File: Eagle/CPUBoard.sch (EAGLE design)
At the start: 33 parts, among them IC2 MAX232, IC3 MAX485CPA, J1 DISPLAY, J2 BUTTON_BOARD, J3 RELAY_BOARD, Q1 12.000MHz, X6 MKDSN1,5/3-5,08, X7 MKDSN1,5/3-5,08

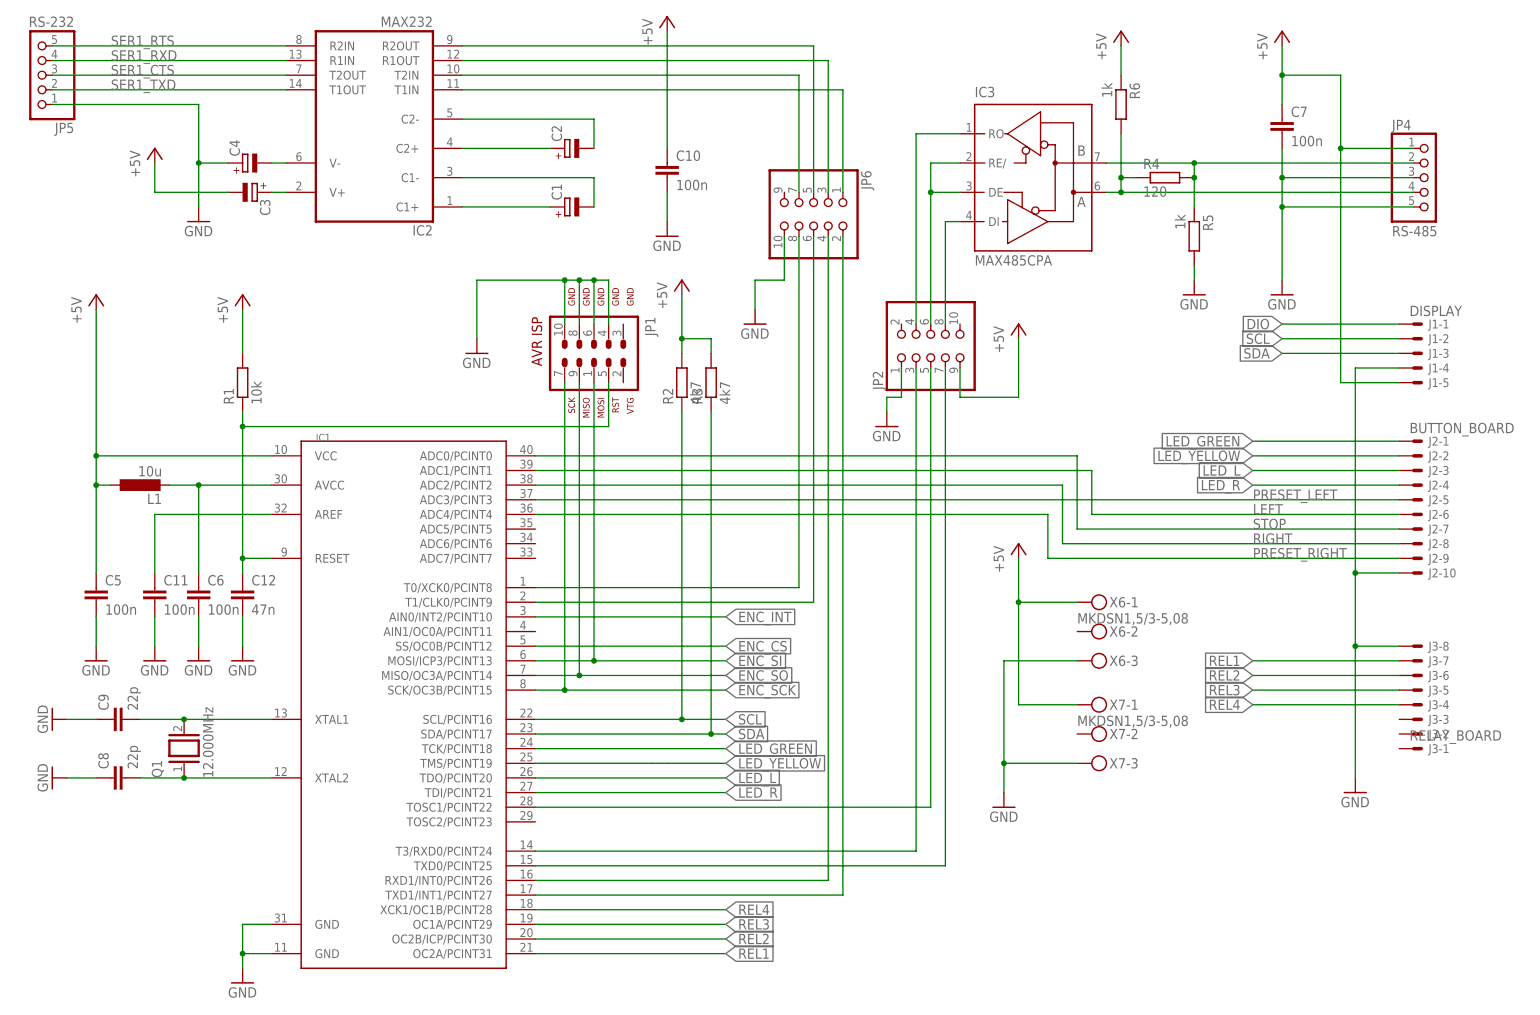
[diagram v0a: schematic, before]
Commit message: - wiring from/to MAX232 changed slightly
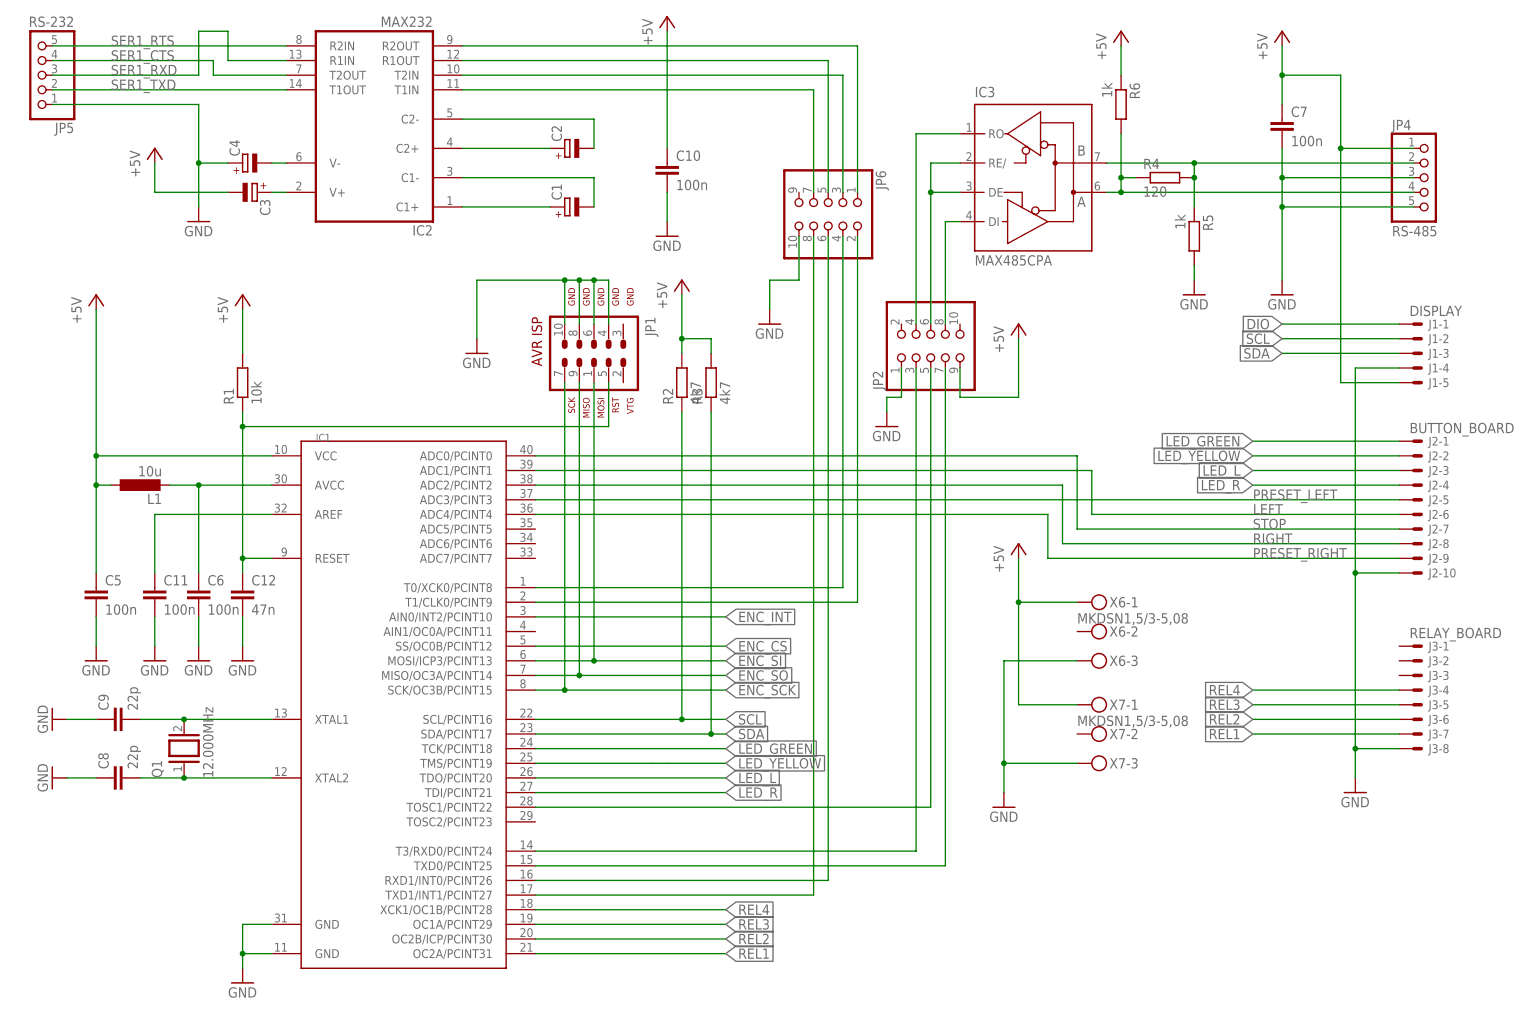
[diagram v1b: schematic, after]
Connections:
- removed net N$30: IC1.T1/CLK0/PCINT9, JP6.6
- removed net N$31: IC1.T0/XCK0/PCINT8, JP6.8
- new net N$22: IC1.RXD1/INT0/PCINT26, JP6.6
- new net N$25: IC1.T1/CLK0/PCINT9, JP6.2
- net N$11: now also JP6.5; no longer JP6.3
- net N$16: now also IC1.T0/XCK0/PCINT8; no longer IC1.RXD1/INT0/PCINT26
- net N$24: now also JP6.8; no longer JP6.2
- net N$28: now also JP6.1; no longer JP6.5
- net N$29: now also JP6.3; no longer JP6.7
- net N$4: now also JP6.7; no longer JP6.1
- net SER1_CTS: now also IC2G$1.R1IN; no longer IC2G$1.T2OUT
- net SER1_RXD: now also IC2G$1.T2OUT; no longer IC2G$1.R1IN
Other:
- moved on the sheet: J3-1, J3-2, J3-3, J3-4, J3-5, J3-6, J3-7, J3-8, JP6

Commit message: - another fix for the TWI pins, hopefully the last one!
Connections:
- net SCL: now also J1-3.S; no longer J1-2.S
- net SDA: now also J1-2.S; no longer J1-3.S
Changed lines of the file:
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@@
 </segment>
 <segment>
-<label x="220.98" y="121.92" size="1.778" layer="95" rot="MR0" xref="yes"/>
-<wire x1="241.3" y1="121.92" x2="220.98" y2="121.92" width="0.1524" layer="91"/>
-<pinref part="J1" gate="-2" pin="S"/>
+<label x="220.98" y="119.38" size="1.778" layer="95" rot="MR0" xref="yes"/>
+<wire x1="241.3" y1="119.38" x2="220.98" y2="119.38" width="0.1524" layer="91"/>
+<pinref part="J1" gate="-3" pin="S"/>
 </segment>
 </net>
@@
 </segment>
 <segment>
-<label x="220.98" y="119.38" size="1.778" layer="95" rot="MR0" xref="yes"/>
-<wire x1="241.3" y1="119.38" x2="220.98" y2="119.38" width="0.1524" layer="91"/>
-<pinref part="J1" gate="-3" pin="S"/>
+<label x="220.98" y="121.92" size="1.778" layer="95" rot="MR0" xref="yes"/>
+<pinref part="J1" gate="-2" pin="S"/>
+<wire x1="220.98" y1="121.92" x2="241.3" y2="121.92" width="0.1524" layer="91"/>
 </segment>
 </net>

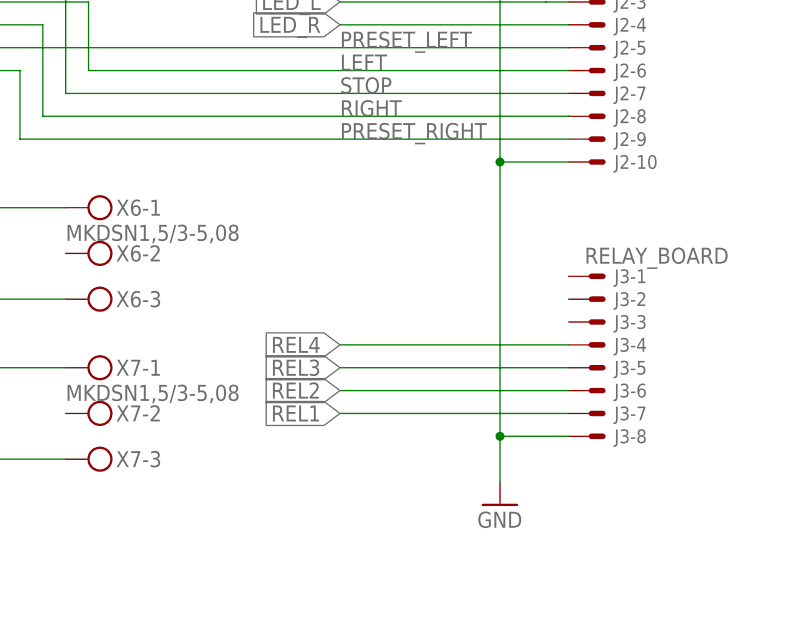
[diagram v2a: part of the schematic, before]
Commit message: - swapped connections to relay board1
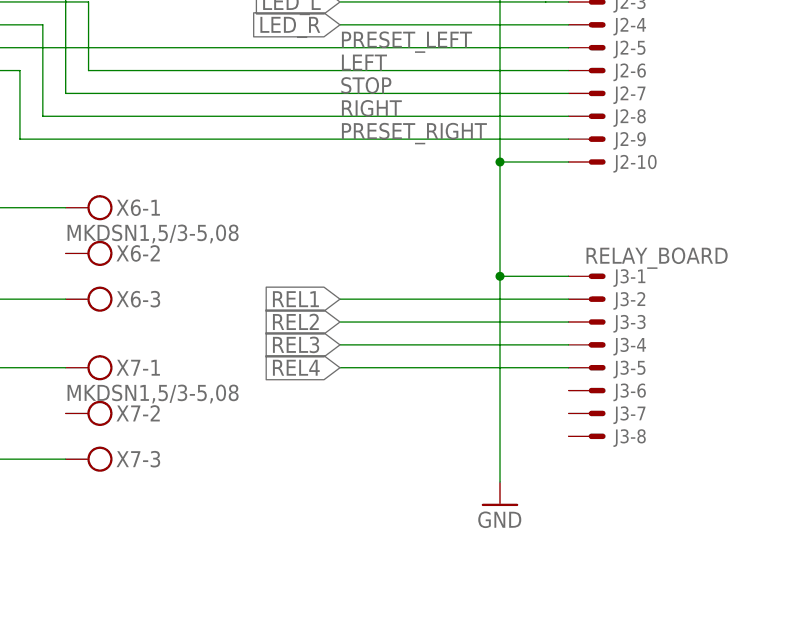
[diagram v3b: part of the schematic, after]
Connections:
- net GND: now also J3-1.S; no longer J3-8.S
- net REL1: now also J3-2.S; no longer J3-7.S
- net REL2: now also J3-3.S; no longer J3-6.S
- net REL3: now also J3-4.S; no longer J3-5.S
- net REL4: now also J3-5.S; no longer J3-4.S
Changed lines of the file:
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@@
 <segment>
 <pinref part="GND11" gate="1" pin="GND"/>
-<wire x1="233.68" y1="45.72" x2="233.68" y2="50.8" width="0.1524" layer="91"/>
-<wire x1="233.68" y1="50.8" x2="233.68" y2="81.28" width="0.1524" layer="91"/>
+<wire x1="233.68" y1="45.72" x2="233.68" y2="68.58" width="0.1524" layer="91"/>
+<wire x1="233.68" y1="68.58" x2="233.68" y2="81.28" width="0.1524" layer="91"/>
 <wire x1="241.3" y1="81.28" x2="233.68" y2="81.28" width="0.1524" layer="91"/>
 <wire x1="233.68" y1="116.84" x2="233.68" y2="81.28" width="0.1524" layer="91"/>
@@
 <pinref part="J1" gate="-4" pin="S"/>
 <pinref part="J2" gate="-10" pin="S"/>
-<pinref part="J3" gate="-8" pin="S"/>
-<wire x1="241.3" y1="50.8" x2="233.68" y2="50.8" width="0.1524" layer="91"/>
-<junction x="233.68" y="50.8"/>
+<pinref part="J3" gate="-1" pin="S"/>
+<wire x1="241.3" y1="68.58" x2="233.68" y2="68.58" width="0.1524" layer="91"/>
+<junction x="233.68" y="68.58"/>
 </segment>
 <segment>
@@
 <net name="REL1" class="0">
 <segment>
-<label x="215.9" y="53.34" size="1.778" layer="95" rot="MR0" xref="yes"/>
-<pinref part="J3" gate="-7" pin="S"/>
-<wire x1="215.9" y1="53.34" x2="241.3" y2="53.34" width="0.1524" layer="91"/>
+<label x="215.9" y="66.04" size="1.778" layer="95" rot="MR0" xref="yes"/>
+<pinref part="J3" gate="-2" pin="S"/>
+<wire x1="215.9" y1="66.04" x2="241.3" y2="66.04" width="0.1524" layer="91"/>
 </segment>
 <segment>
@@
 <net name="REL2" class="0">
 <segment>
-<label x="215.9" y="55.88" size="1.778" layer="95" rot="MR0" xref="yes"/>
-<pinref part="J3" gate="-6" pin="S"/>
-<wire x1="241.3" y1="55.88" x2="215.9" y2="55.88" width="0.1524" layer="91"/>
+<label x="215.9" y="63.5" size="1.778" layer="95" rot="MR0" xref="yes"/>
+<wire x1="241.3" y1="63.5" x2="215.9" y2="63.5" width="0.1524" layer="91"/>
+<pinref part="J3" gate="-3" pin="S"/>
 </segment>
 <segment>
@@
 <net name="REL3" class="0">
 <segment>
-<label x="215.9" y="58.42" size="1.778" layer="95" rot="MR0" xref="yes"/>
-<pinref part="J3" gate="-5" pin="S"/>
-<wire x1="215.9" y1="58.42" x2="241.3" y2="58.42" width="0.1524" layer="91"/>
+<label x="215.9" y="60.96" size="1.778" layer="95" rot="MR0" xref="yes"/>
+<pinref part="J3" gate="-4" pin="S"/>
+<wire x1="215.9" y1="60.96" x2="241.3" y2="60.96" width="0.1524" layer="91"/>
 </segment>
 <segment>
@@
 <net name="REL4" class="0">
 <segment>
-<label x="215.9" y="60.96" size="1.778" layer="95" rot="MR0" xref="yes"/>
-<pinref part="J3" gate="-4" pin="S"/>
-<wire x1="215.9" y1="60.96" x2="241.3" y2="60.96" width="0.1524" layer="91"/>
-</segment>
-<segment>
+<label x="215.9" y="58.42" size="1.778" layer="95" rot="MR0" xref="yes"/>
+<wire x1="215.9" y1="58.42" x2="241.3" y2="58.42" width="0.1524" layer="91"/>
+<pinref part="J3" gate="-5" pin="S"/>
+</segment>
+<segment>

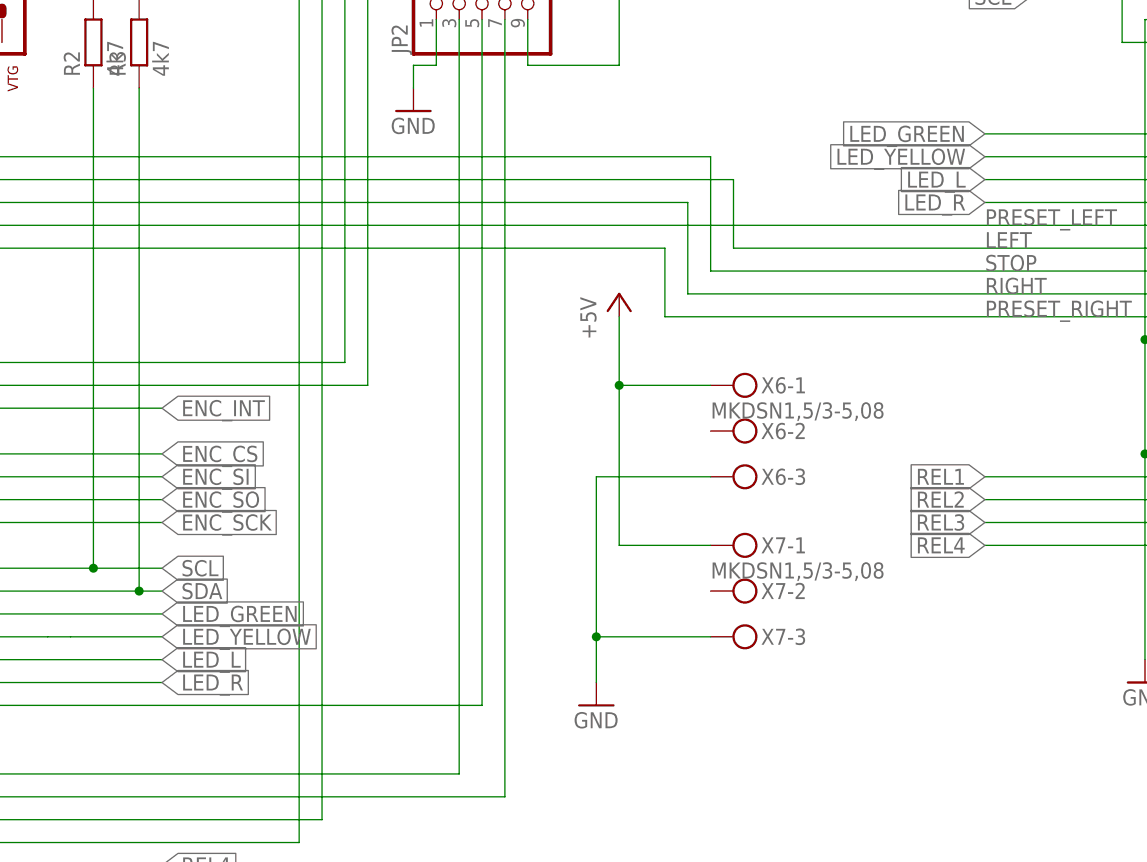
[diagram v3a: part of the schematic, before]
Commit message: - swapped LED_L and LED_R in schematic - solder bridge between two buttons found and fixed
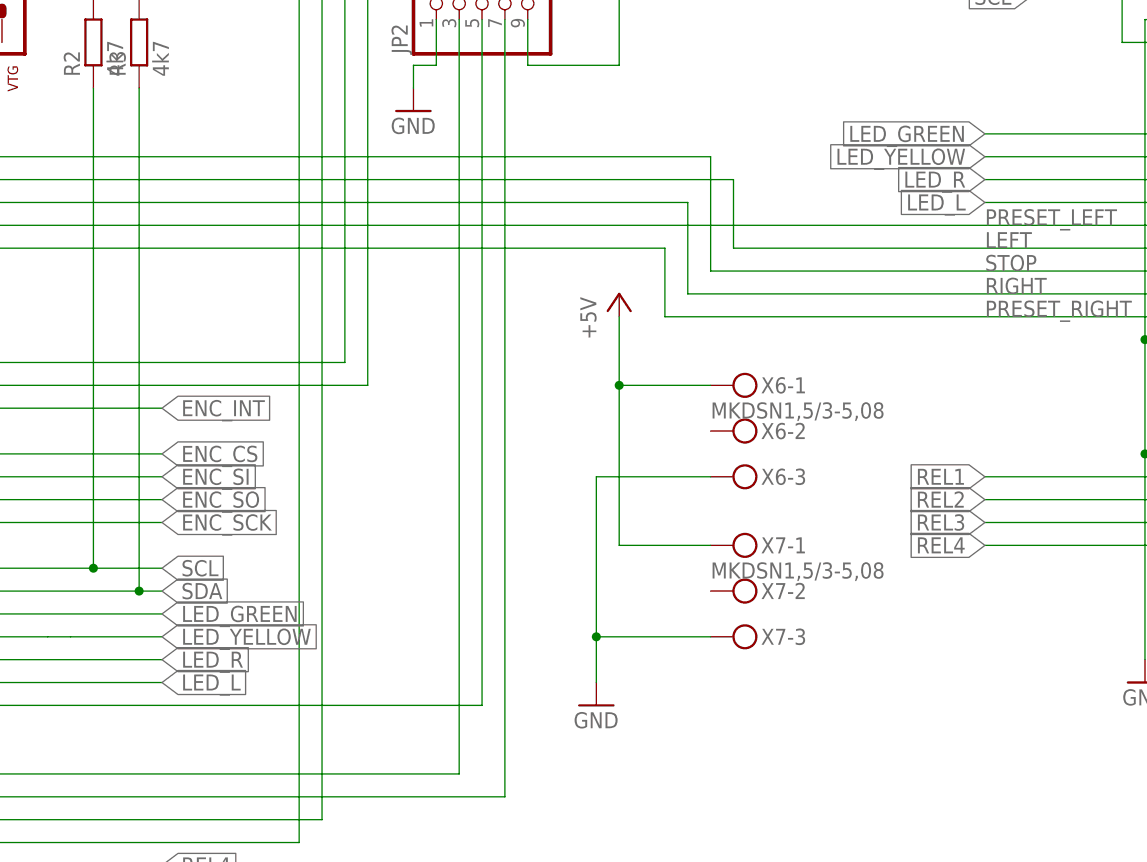
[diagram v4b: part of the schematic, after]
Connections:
- net LED_L: now also IC1.TDI/PCINT21, J2-4.S; no longer IC1.TDO/PCINT20, J2-3.S
- net LED_R: now also IC1.TDO/PCINT20, J2-3.S; no longer IC1.TDI/PCINT21, J2-4.S
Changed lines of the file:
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@@
 <net name="LED_L" class="0">
+<segment>
+<label x="124.46" y="43.18" size="1.778" layer="95" xref="yes"/>
+<pinref part="IC1" gate="G$1" pin="TDI/PCINT21"/>
+<wire x1="91.44" y1="43.18" x2="124.46" y2="43.18" width="0.1524" layer="91"/>
+</segment>
+<segment>
+<wire x1="241.3" y1="96.52" x2="215.9" y2="96.52" width="0.1524" layer="91"/>
+<label x="215.9" y="96.52" size="1.778" layer="95" rot="MR0" xref="yes"/>
+<pinref part="J2" gate="-4" pin="S"/>
+</segment>
+</net>
+<net name="LED_R" class="0">
+<segment>
+<wire x1="91.44" y1="45.72" x2="124.46" y2="45.72" width="0.1524" layer="91"/>
+<label x="124.46" y="45.72" size="1.778" layer="95" xref="yes"/>
+<pinref part="IC1" gate="G$1" pin="TDO/PCINT20"/>
+</segment>
 <segment>
 <wire x1="241.3" y1="99.06" x2="238.76" y2="99.06" width="0.1524" layer="91"/>
@@
 <wire x1="238.76" y1="99.06" x2="215.9" y2="99.06" width="0.1524" layer="91"/>
 </segment>
-<segment>
-<wire x1="91.44" y1="45.72" x2="124.46" y2="45.72" width="0.1524" layer="91"/>
-<label x="124.46" y="45.72" size="1.778" layer="95" xref="yes"/>
-<pinref part="IC1" gate="G$1" pin="TDO/PCINT20"/>
-</segment>
 </net>
-<net name="LED_R" class="0">
-<segment>
-<wire x1="241.3" y1="96.52" x2="215.9" y2="96.52" width="0.1524" layer="91"/>
-<label x="215.9" y="96.52" size="1.778" layer="95" rot="MR0" xref="yes"/>
-<pinref part="J2" gate="-4" pin="S"/>
-</segment>
-<segment>
-<label x="124.46" y="43.18" size="1.778" layer="95" xref="yes"/>
-<pinref part="IC1" gate="G$1" pin="TDI/PCINT21"/>
-<wire x1="91.44" y1="43.18" x2="124.46" y2="43.18" width="0.1524" layer="91"/>
-</segment>
-</net>
